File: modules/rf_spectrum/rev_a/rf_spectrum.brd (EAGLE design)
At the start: 68.1 x 66 mm, 44 parts, among them J1 MODULE_GENERIC, J7 TC2030-JLINK-L, P1 MOLEX_73251-135X, P2 MOLEX_73251-135X, P3 MOLEX_73251-135X, U1 SAM4LC8AA, U2 MWSUB3G, U3 SKY13317, U7 TLV62130, X1 16MHz

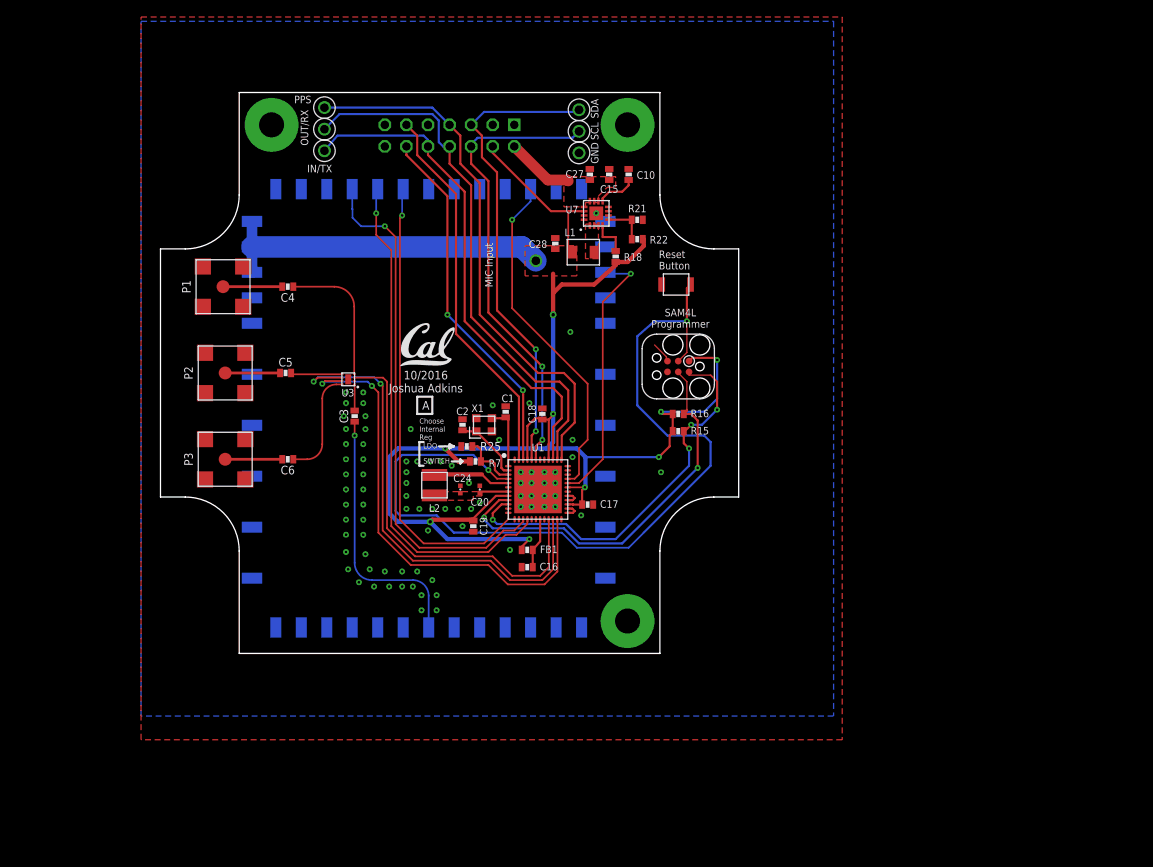
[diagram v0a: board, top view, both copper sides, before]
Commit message: schematic done, much routing done
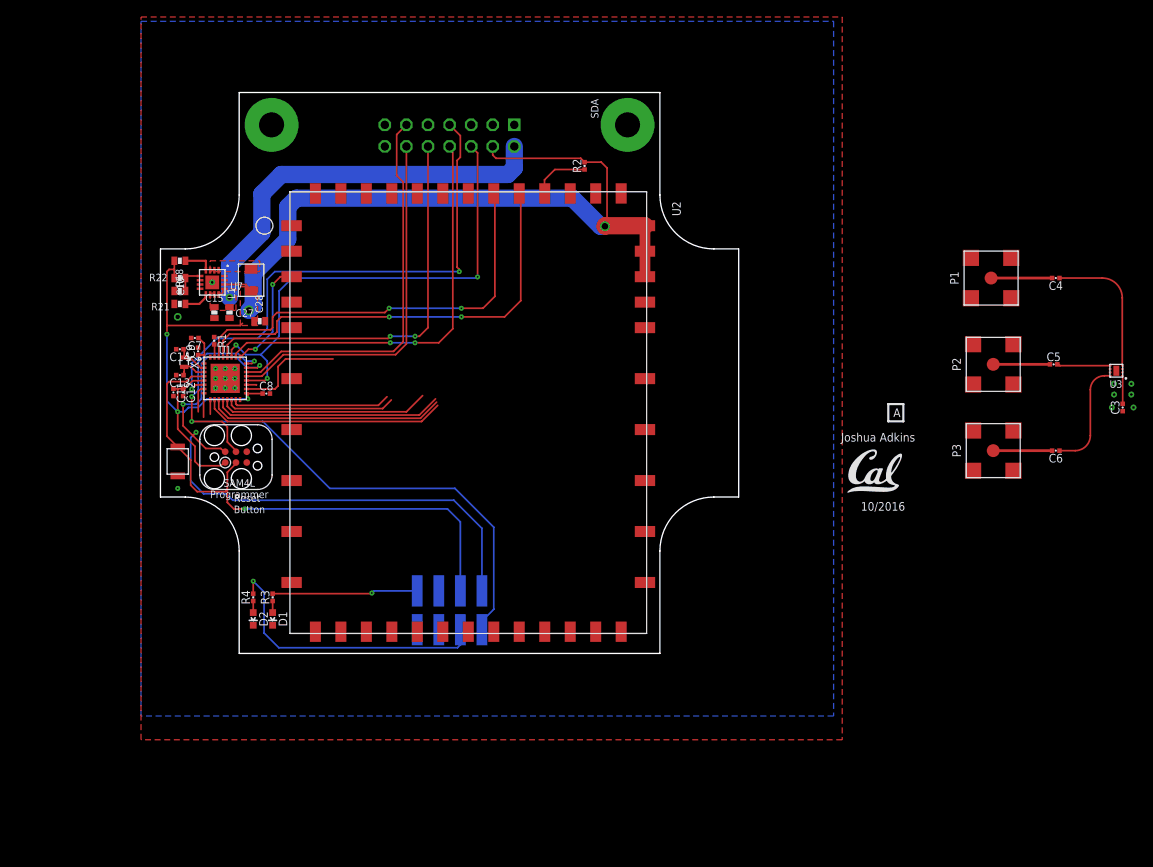
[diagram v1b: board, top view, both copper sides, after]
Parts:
- removed C1, C2: 8pF, passives:0603_CAP
- removed C16, C17, C18, C19: 100nF, passives:0603_CAP
- removed C20: 100nF, passives:0402_CAP
- removed C24: 4.7uF, passives:0402_CAP
- removed FB1: 1.5kΩ, passives:0603_CAP
- removed L2: 22uH, signpost:1212
- removed R15, R16: 100k, passives:0603-RES
- removed R25: 0, passives:0603-RES
- removed R7: 10k, passives:0603-RES
- removed TP11, TP12, TP13, TP14, TP15, TP16: TEST_POINT_0.040IN, headers:TESTPOINT_0.040IN
- removed X1: 16MHz, crystals:FHXXX
- added C11: 10nF, passives:0402_CAP
- added C12: 1uF, passives:0402_CAP
- added C13, C14: 4.3pF, passives:0402_CAP
- added C7: 4.7uF, passives:0402_CAP
- added C8, C9: 100nF, passives:0402_CAP
- added D1: GREEN, leds:LED-0603
- added D2: RED, leds:LED-0603
- added R1, R3, R4: 10k, passives:0402_RES
- added R2: 100k, passives:0402_RES
- added X2: ABS05-32.768KHZ-9-T, crystals:ABS05
- C3, C4, C5, C6: device passives:0603_CAP -> passives:0402_CAP
- J1: value MODULE_GENERIC -> MODULE_GENERIC_DEBUGSMT; device signpost:MODULE_GENERIC -> signpost:MODULE_GENERIC_DEBUG_SMT
- U1: value SAM4LC8AA -> STM32L432KC; device chips:QFN-48-7MM -> chips:UQFN-32
- moved C3 90.4 mm to (115.8, 31.5)
- moved C4 90.4 mm to (108.0, 46.7)
- moved C5 90.4 mm to (107.7, 36.6)
- moved C6 90.4 mm to (108.0, 26.4)
- moved P2 90.4 mm to (100.6, 36.6)
- moved P3 90.4 mm to (100.6, 26.4)
- moved U3 90.4 mm to (115.8, 36.6)
- moved P1 90.4 mm to (100.3, 46.7)
- moved S1 62.3 mm to (4.57, 25.1), turned to 90 degrees
- moved C10 55.0 mm to (4.83, 43.7), turned to 0 degrees
- moved U$2 54.7 mm to (83.4, 21.4)
- moved R21 54.5 mm to (4.83, 45.2), turned to 0 degrees
- moved R22 54.0 mm to (4.83, 46.7), turned to 180 degrees
- moved J7 53.2 mm to (11.4, 25.7), turned to 0 degrees
- moved R18 51.3 mm to (4.83, 48.8), turned to 180 degrees
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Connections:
- removed net !CONTROLLER_RESET: J7.3, S1.2, U1.4
- removed net CONTROLLER_BUCK/LDO_N: R25.2, R7.1, U1.3
- removed net CONTROLLER_SWDCLK: J7.4, R16.1, U1.9
- removed net CONTROLLER_SWDIO: J7.2, R15.1, U1.10
- removed net CONTROLLER_XIN: C1.1, U1.1, X1.3
- removed net CONTROLLER_XOUT: C2.1, U1.2, X1.1
- removed net N$32: C16.1, FB1.1, U1.19
- removed net N$44: C20.1, C24.1, L2.P$1, U1.7
- removed net N$52: L2.P$2, U1.5
- removed net N$53: U1.28, U1.29
- removed net N$54: U1.25, U1.26
- new net !RST: J1.20, J7.3, S1.2, U1.P$4
- new net DBG_GPIO1: J1.16, R3.2, U1.P$14
- new net DBG_GPIO2: J1.19, R4.2, U1.P$15
- new net DBG_RX: J1.18, U1.P$9
- new net DBG_TX: J1.17, U1.P$8
- new net N$10: C13.1, U1.P$3, X2.B
- new net N$11: R1.2, U1.P$31
- new net N$12: D1.A, R3.1
- new net N$13: D2.A, R4.1
- new net N$9: C14.1, U1.P$2, X2.A
- new net SWDCLK: J1.21, J7.4, U1.P$24
- new net SWDIO: J1.22, J7.2, U1.P$23
- net 3V3: now also C11.1, C12.1, C7.1, C8.1, C9.1, R2.2, U1.P$1, U1.P$17, U1.P$5; no longer C17.1, C18.1, C19.1, FB1.2, R15.2, R16.2, R7.2, U1.27, U1.31, U1.40, U1.45, U1.8
- net GND: now also C11.2, C12.2, C13.2, C14.2, C7.2, C8.2, C9.2, D1.C, D2.C, J1.15, R1.1, U1.P$16, U1.P$32, U1.P$33; no longer C1.2, C16.2, C17.2, C18.2, C19.2, C2.2, C20.2, C24.2, R25.1, TP11.TESTPOINT, U1.17, U1.30, U1.48, U1.6, U1.THERMAL, X1.2, X1.4
- net MOD_IN: now also U1.P$28; no longer TP14.TESTPOINT, U1.39
- net MOD_OUT: now also U1.P$26; no longer TP15.TESTPOINT, U1.38
- net PPS: now also U1.P$6; no longer TP16.TESTPOINT, U1.37
- net RF_ANT1: now also U1.P$10; no longer U1.21
- net RF_ANT2: now also U1.P$11; no longer U1.22
- net RF_ANT3: now also U1.P$12; no longer U1.23
- net RF_GPIO2: now also U1.P$25; no longer U1.32
- net RF_GPIO3: now also R2.1, U1.P$7; no longer U1.15
- net RF_RESET: now also U1.P$18; no longer U1.33
- net RF_RX: now also U1.P$29; no longer U1.16
- net RF_TX: now also U1.P$30; no longer U1.12
- net SCL: now also U1.P$13, U1.P$19; no longer TP12.TESTPOINT, U1.44
- net SDA: now also U1.P$20, U1.P$27; no longer TP13.TESTPOINT, U1.43
- net USB+: now also U1.P$22; no longer U1.47
- net USB-: now also U1.P$21; no longer U1.46
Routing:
- net !CONTROLLER_RESET: track 100.9 -> 0.00 mm, vias 2 -> 0
- net SWDCLK: track 0.00 -> 76.9 mm, vias 0 -> 3
- net SWDIO: track 0.00 -> 75.3 mm, vias 0 -> 3
- net !RST: track 0.00 -> 64.2 mm, vias 0 -> 1
- net 3V3: track 212.9 -> 151.6 mm, vias 10 -> 5
- net DBG_GPIO2: track 0.00 -> 52.7 mm, vias 0 -> 1
- net RF_GPIO3: track 60.9 -> 10.1 mm, vias 1 -> 0
- net CONTROLLER_SWDIO: track 47.3 -> 0.00 mm, vias 4 -> 0
- net CONTROLLER_SWDCLK: track 47.2 -> 0.00 mm, vias 2 -> 0
- net 5V: track 8.05 -> 47.6 mm, vias 0 -> 1
- net DBG_GPIO1: track 0.00 -> 37.2 mm, vias 0 -> 1
- net N$1: track 30.7 -> 0.00 mm, vias 1 -> 0
- net RF_ANT2: track 58.2 -> 28.0 mm, vias 2 -> 0
- net SCL: track 56.2 -> 26.0 mm, vias 2 -> 0
- net RF_ANT3: track 56.6 -> 27.1 mm, vias 2 -> 0
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- removed copper zone on layer 1, net N$44
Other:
- board text removed: "Choose Internal Reg"
- board text removed: "GND"
- board text removed: "IN/TX"
- board text removed: "LDO"
- board text removed: "MIC Input"
- board text removed: "OUT/RX"
- board text removed: "PPS"
- board text removed: "SCL"
- board text removed: "SWITCH"

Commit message: finished routing, no silk yet
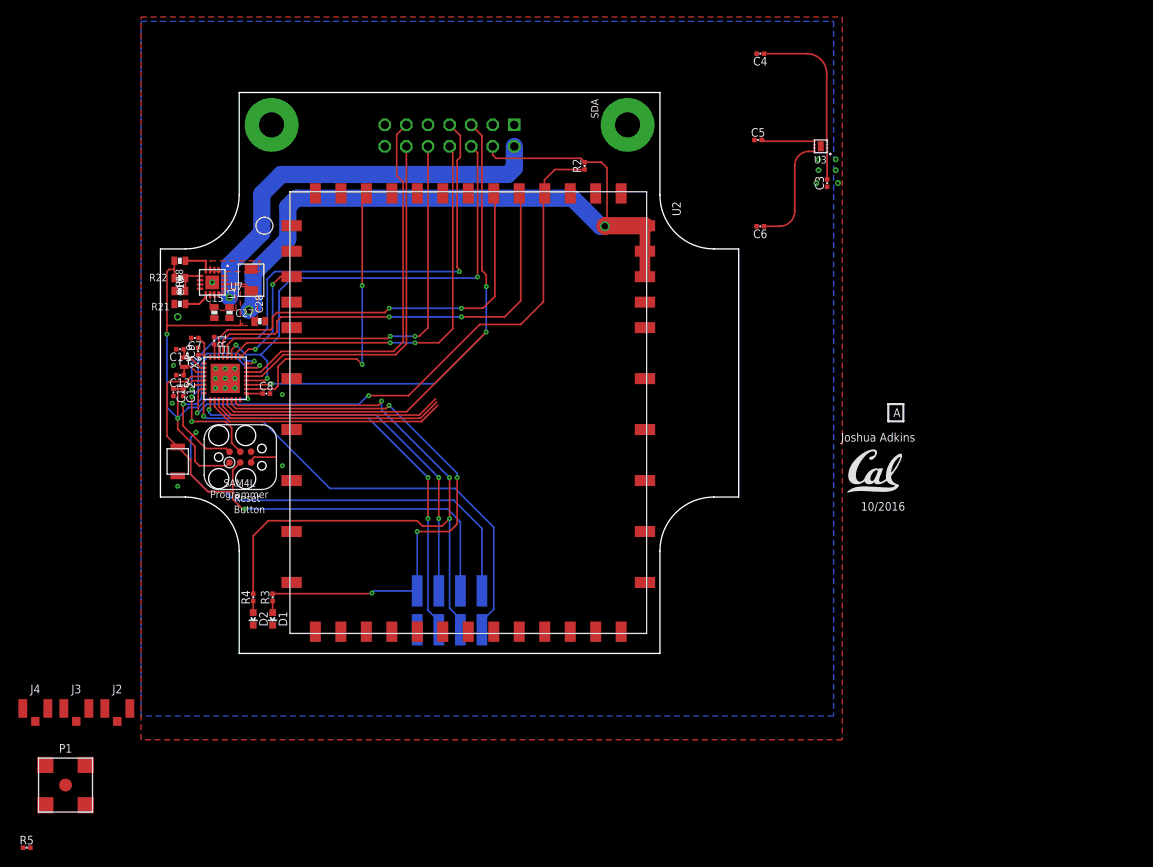
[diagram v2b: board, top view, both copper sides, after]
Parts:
- removed P2, P3: MOLEX_73251-135X, connector:SMA-J/PCB
- added J2, J3, J4: U.FL-R-SMT, connector:U.FL_SMT
- added R5: 0, passives:0402_RES
- moved P1 124.2 mm to (-8.64, -13.0), turned to 0 degrees
- moved C3 43.7 mm to (81.0, 57.9)
- moved C4 43.7 mm to (73.2, 73.2)
- moved C5 43.7 mm to (72.9, 63.0)
- moved C6 43.7 mm to (73.2, 52.8)
- moved U3 43.7 mm to (81.0, 63.0)
- moved J7 0.51 mm to (11.9, 25.7)
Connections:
- new net N$14: P1.1, R5.2
- net GND: now also J2.GND1, J2.GND2, J3.GND1, J3.GND2, J4.GND1, J4.GND2; no longer P2.2, P2.3, P2.4, P2.5, P3.2, P3.3, P3.4, P3.5
- net N$1: now also R5.1
- net N$4: now also J2.SIG; no longer P1.1
- net N$6: now also J3.SIG; no longer P2.1
- net N$8: now also J4.SIG; no longer P3.1
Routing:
- net SCL: track 26.0 -> 91.3 mm, vias 0 -> 3
- net RF_GPIO3: track 10.1 -> 69.3 mm, vias 0 -> 2
- net DBG_TX: track 2.87 -> 50.6 mm, vias 0 -> 3
- net DBG_RX: track 1.72 -> 45.2 mm, vias 0 -> 3
- net DBG_GPIO2: track 52.7 -> 81.8 mm, vias 1 -> 3
- net DBG_GPIO1: track 37.2 -> 66.0 mm, vias 1 -> 4
- net RF_RESET: track 13.0 -> 37.0 mm, vias 0 -> 2
- net N$4: track 7.19 -> 0.00 mm
- net N$8: track 6.93 -> 0.00 mm
- net N$6: track 6.68 -> 0.00 mm
- net GND: track 0.00 -> 4.25 mm, vias 20 -> 24
- net 3V3: track 151.6 -> 153.1 mm
- net !RST: track 64.2 -> 63.1 mm

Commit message: added labels
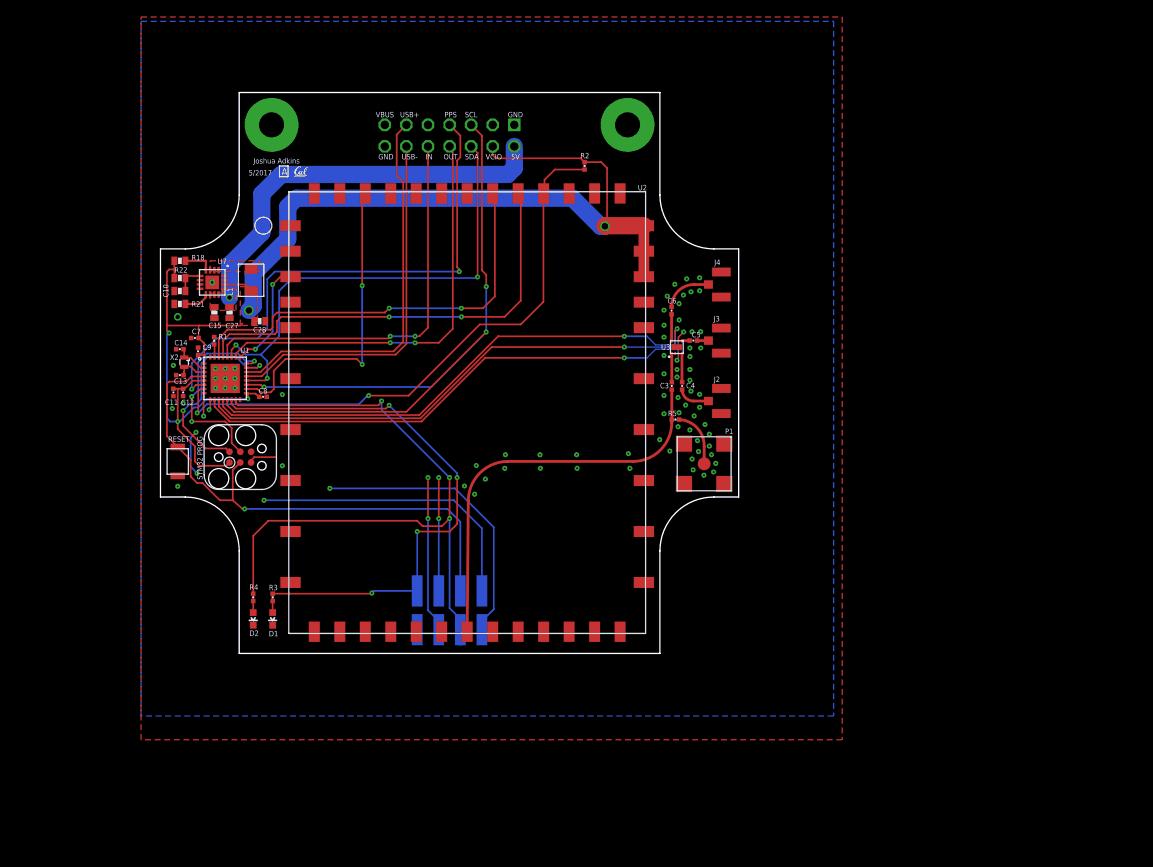
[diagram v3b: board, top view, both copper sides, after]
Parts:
- U$2: device logos:UCB_CAL_200MIL -> logos:UCB_CAL_50MIL
- moved J4 94.9 mm to (68.6, 46.0), turned to 270 degrees
- moved R5 91.5 mm to (63.2, 30.1)
- moved J3 87.4 mm to (68.6, 39.4), turned to 270 degrees
- moved P1 84.2 mm to (66.5, 24.9)
- moved J2 79.8 mm to (68.6, 32.3), turned to 270 degrees
- moved U$2 75.0 mm to (18.2, 58.7)
- moved C4 40.2 mm to (64.0, 34.0), turned to 270 degrees
- moved U3 30.3 mm to (64.1, 37.8), turned to 90 degrees
- moved C3 30.1 mm to (62.7, 34.0)
- moved C5 24.8 mm to (65.3, 39.4), turned to 180 degrees
- moved C6 14.4 mm to (62.7, 42.9), turned to 90 degrees
- moved C8 0.54 mm to (14.6, 32.8)
- moved U2 0.13 mm to (17.7, 56.9)
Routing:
- net N$1: track 0.00 -> 47.1 mm
- net RF_ANT3: track 27.0 -> 62.2 mm, vias 0 -> 2
- net RF_ANT2: track 27.8 -> 62.2 mm, vias 0 -> 2
- net RF_ANT1: track 28.6 -> 61.8 mm, vias 0 -> 2
- net N$3: track 16.3 -> 3.41 mm
- net N$7: track 12.8 -> 3.16 mm
- net N$14: track 0.00 -> 6.36 mm
- net N$8: track 0.00 -> 5.44 mm
- net N$5: track 6.27 -> 0.93 mm
- net N$4: track 0.00 -> 3.65 mm
- net 3V3: track 153.1 -> 155.6 mm
- net N$6: track 0.00 -> 1.34 mm
- net SWDIO: track 75.4 -> 74.7 mm, vias 3 -> 5
- net !RST: track 63.1 -> 63.7 mm
- net SWDCLK: vias 3 -> 4
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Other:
- board text added: "5/2017"
- board text added: "5V"
- board text added: "GND"
- board text added: "IN"
- board text added: "OUT"
- board text added: "PPS"
- board text added: "RESET"
- board text added: "SCL"
- board text added: "STM32 PROG"
- board text added: "USB+"
- board text added: "USB-"
- board text added: "VBUS"
- board text added: "VCIO"
- board text removed: "10/2016"
- board text removed: "Reset Button"
- board text removed: "SAM4L Programmer"

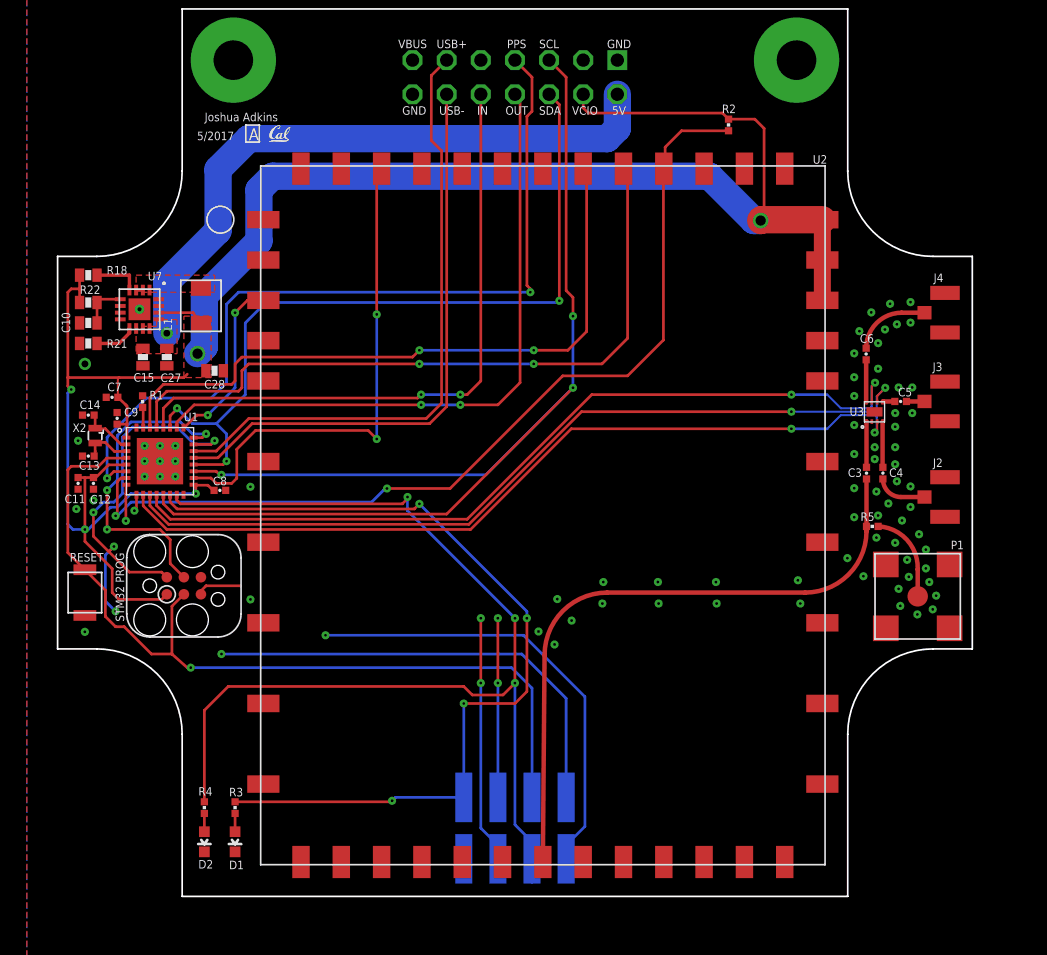
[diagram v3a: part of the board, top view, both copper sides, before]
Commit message: added debug signals and better labels
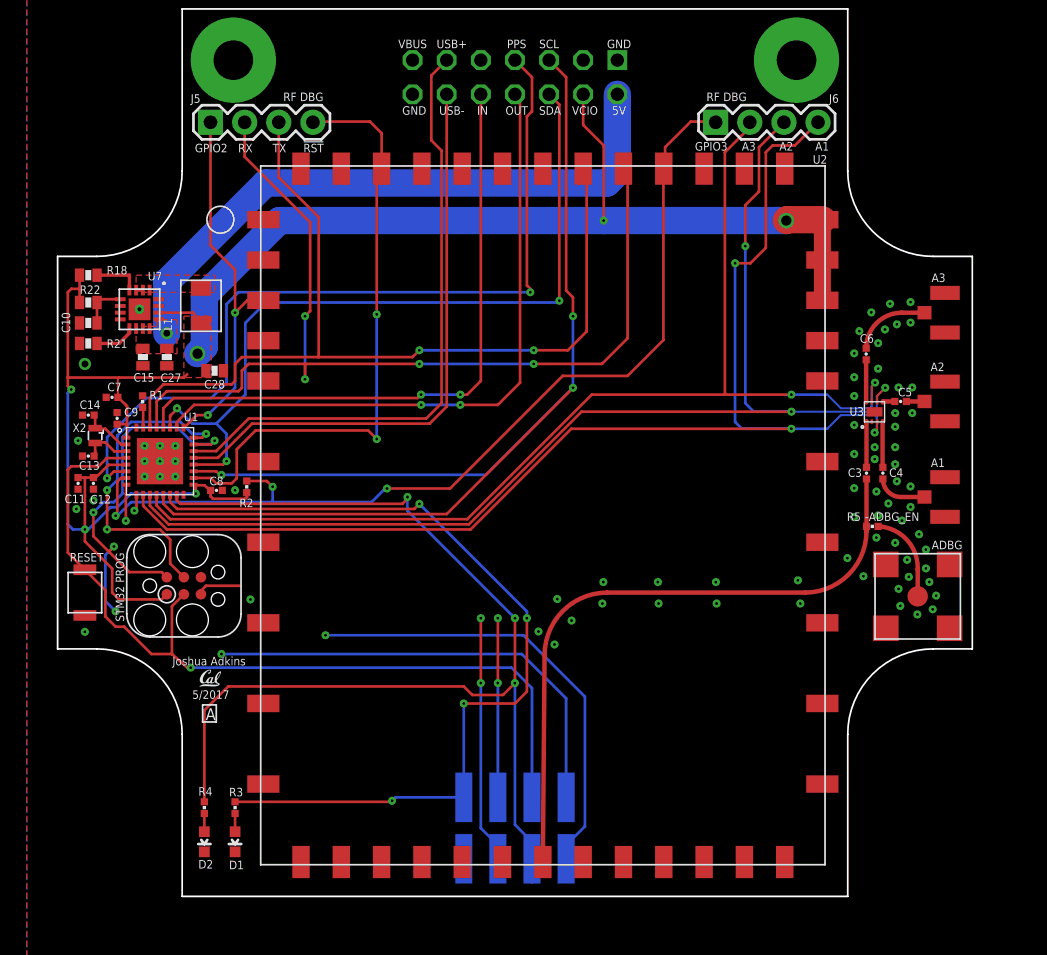
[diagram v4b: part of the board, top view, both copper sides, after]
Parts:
- added J5, J6: (no value), SparkFun-Connectors:1X04
- moved R2 44.8 mm to (16.6, 33.0), turned to 270 degrees
- moved U$2 40.8 mm to (13.1, 18.1)
- moved C8 0.25 mm to (14.4, 32.8)
- renumbered J2 to A1, J3 to A2, J4 to A3, P1 to ADBG
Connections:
- removed net RF_RESET: U1.P$18, U2.P$44
- new net !RF_RESET: J5.4, U1.P$18, U2.P$44
- net RF_ANT1: now also J6.4
- net RF_ANT2: now also J6.3
- net RF_ANT3: now also J6.2
- net RF_GPIO2: now also J5.1
- net RF_GPIO3: now also J6.1
- net RF_RX: now also J5.2
- net RF_TX: now also J5.3
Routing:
- net !RF_RESET: track 0.00 -> 45.3 mm, vias 0 -> 2
- net RF_RESET: track 37.2 -> 0.00 mm, vias 2 -> 0
- net RF_ANT1: track 61.8 -> 92.7 mm, vias 2 -> 3
- net RF_ANT2: track 62.2 -> 88.0 mm, vias 2 -> 3
- net RF_RX: track 52.5 -> 74.9 mm, vias 2 -> 4
- net RF_ANT3: track 62.2 -> 83.2 mm
- net RF_TX: track 49.8 -> 68.5 mm
- net RF_GPIO2: track 13.1 -> 28.1 mm
- net 3V3: track 155.6 -> 142.2 mm, vias 5 -> 6
- net RF_GPIO3: track 69.3 -> 71.8 mm, vias 2 -> 3
- net 5V: track 47.6 -> 46.8 mm
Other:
- board text added: "!RST"
- board text added: "-ADBG_EN"
- board text added: "A1"
- board text added: "A2"
- board text added: "A3"
- board text added: "GPIO2"
- board text added: "GPIO3"
- board text added: "RF DBG"
- board text added: "RX"
- board text added: "TX"
